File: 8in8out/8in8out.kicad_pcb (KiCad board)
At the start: 2 copper layers, 122 parts, among them IC1 ATTINY2313-P, J1 RJ45, J2 RJ45, J3 CONN_6, K110 G5T-1-12VDC, K120 G5T-1-12VDC, K130 G5T-1-12VDC, K140 G5T-1-12VDC, K150 G5T-1-12VDC, K160 G5T-1-12VDC, K170 G5T-1-12VDC, K180 G5T-1-12VDC, P1 CONN_5, P100 CONN_2, P101 CONN_2, P102 CONN_2, P103 CONN_2, P105 CONN_2, P106 CONN_2, P107 CONN_3, P109 CONN_2, P110 CONN_2, P120 CONN_2, P130 CONN_2, P140 CONN_2, P150 CONN_2, P160 CONN_2, P170 CONN_2, P180 CONN_2, P2 CONN_5, Q110 NPN, Q120 NPN, Q130 NPN, Q140 NPN, Q150 NPN, Q160 NPN, Q170 NPN, Q180 NPN, U1 74HC595, U10 OPTO-TRANSISTOR, U2 74LS165, U20 OPTO-TRANSISTOR, U30 OPTO-TRANSISTOR, U40 OPTO-TRANSISTOR, U50 OPTO-TRANSISTOR, U60 OPTO-TRANSISTOR, U70 OPTO-TRANSISTOR, U80 OPTO-TRANSISTOR

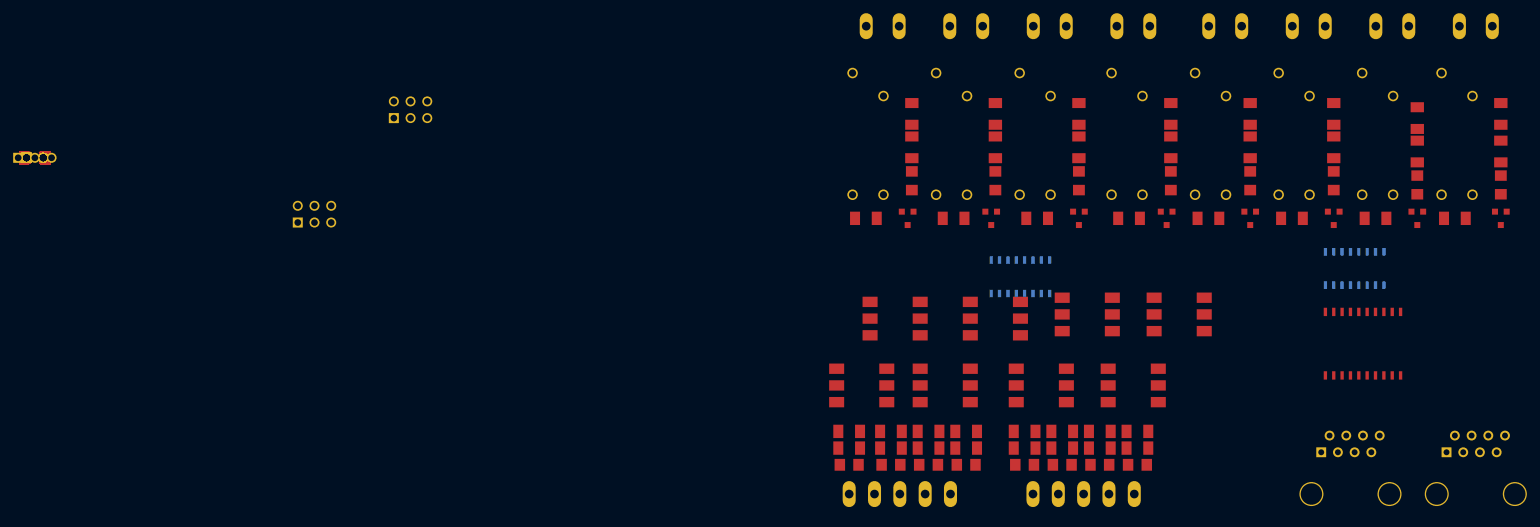
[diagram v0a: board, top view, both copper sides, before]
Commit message: Redimensionnement PCB en 100*86
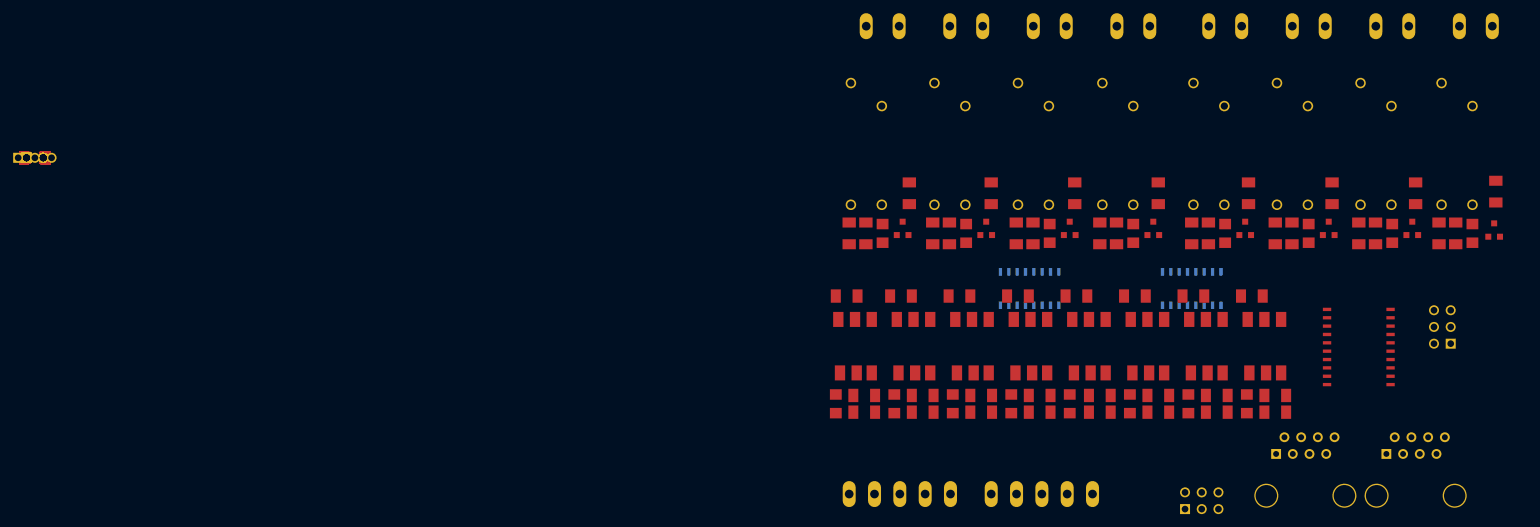
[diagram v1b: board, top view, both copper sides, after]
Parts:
- ISP0: footprint HE10-6 -> pin_array_3x2
- moved R82 186.2 mm to (247.9, 119.8)
- moved R72 177.4 mm to (239.0, 119.8)
- moved ISP0 172.3 mm to (276.9, 124.5), turned to 90 degrees
- moved R62 168.5 mm to (230.1, 119.8)
- moved R52 159.7 mm to (221.2, 119.8)
- moved R42 150.9 mm to (212.3, 119.8)
- moved R32 142.1 mm to (203.5, 119.8)
- moved J3 134.2 mm to (240.3, 150.9)
- moved R22 133.3 mm to (194.6, 119.8)
- moved R12 125.2 mm to (186.3, 119.8)
- moved U1 25.0 mm to (238.8, 118.6), turned to 180 degrees
- moved R80 21.7 mm to (251.5, 137.4), turned to 0 degrees
- moved R81 21.7 mm to (251.5, 134.9), turned to 0 degrees
- moved R141 21.1 mm to (224.8, 110.2)
- moved R111 20.5 mm to (186.7, 110.2)
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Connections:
- P1 pad 5: DGND -> GND
- P2 pad 5: DGND -> GND
- U2 pad 11: (no net) -> CMD0
- U2 pad 12: (no net) -> CMD1
- U2 pad 13: (no net) -> CMD2
- U2 pad 14: (no net) -> CMD3
- U2 pad 3: (no net) -> CMD4
- U2 pad 4: (no net) -> CMD5
- U2 pad 5: (no net) -> CMD6
- U2 pad 6: (no net) -> CMD7

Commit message: Correction pin data du 74HC165 Ajustement position des composants
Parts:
- P105: footprint PIN_ARRAY_2X1 -> MOL_CONN_2_VH
- P107: footprint PIN_ARRAY_3X1 -> PIN_ARRAY_5x1
- moved R4 235.2 mm to (297.4, 116.8)
- moved P103 215.5 mm to (275.6, 133.6), turned to 180 degrees
- moved P102 215.1 mm to (275.6, 131.1), turned to 180 degrees
- moved P101 214.8 mm to (275.6, 128.5), turned to 180 degrees
- moved R2 214.6 mm to (276.1, 123.4), turned to 180 degrees
- moved P100 214.4 mm to (275.6, 126.0), turned to 180 degrees
- moved D2 214.3 mm to (276.1, 120.9)
- moved P106 214.1 mm to (276.1, 118.4)
- moved C2 202.2 mm to (261.6, 136.1), turned to 270 degrees
- moved R1 201.7 mm to (263.9, 115.3), turned to 180 degrees
- moved C1 199.7 mm to (259.1, 136.1), turned to 270 degrees
- moved R3 197.2 mm to (256.5, 136.1), turned to 270 degrees
- moved D3 195.9 mm to (256.5, 128.3), turned to 270 degrees
- moved D1 195.9 mm to (258.1, 115.3), turned to 180 degrees
- moved P109 195.0 mm to (256.5, 121.9), turned to 270 degrees
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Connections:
- U2 pad 10: DATA_IN -> (no net)
- U2 pad 9: (no net) -> DATA_IN

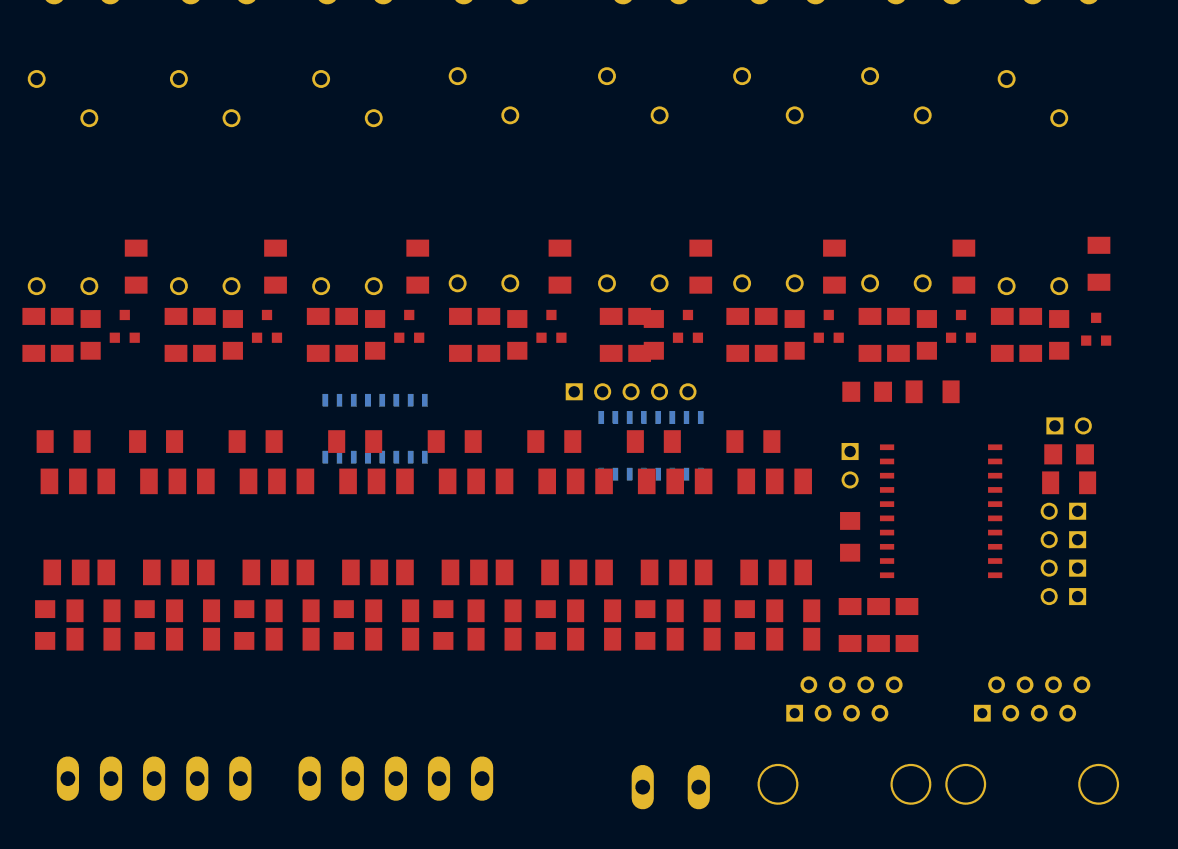
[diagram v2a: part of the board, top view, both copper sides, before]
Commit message: Modification 74HC165
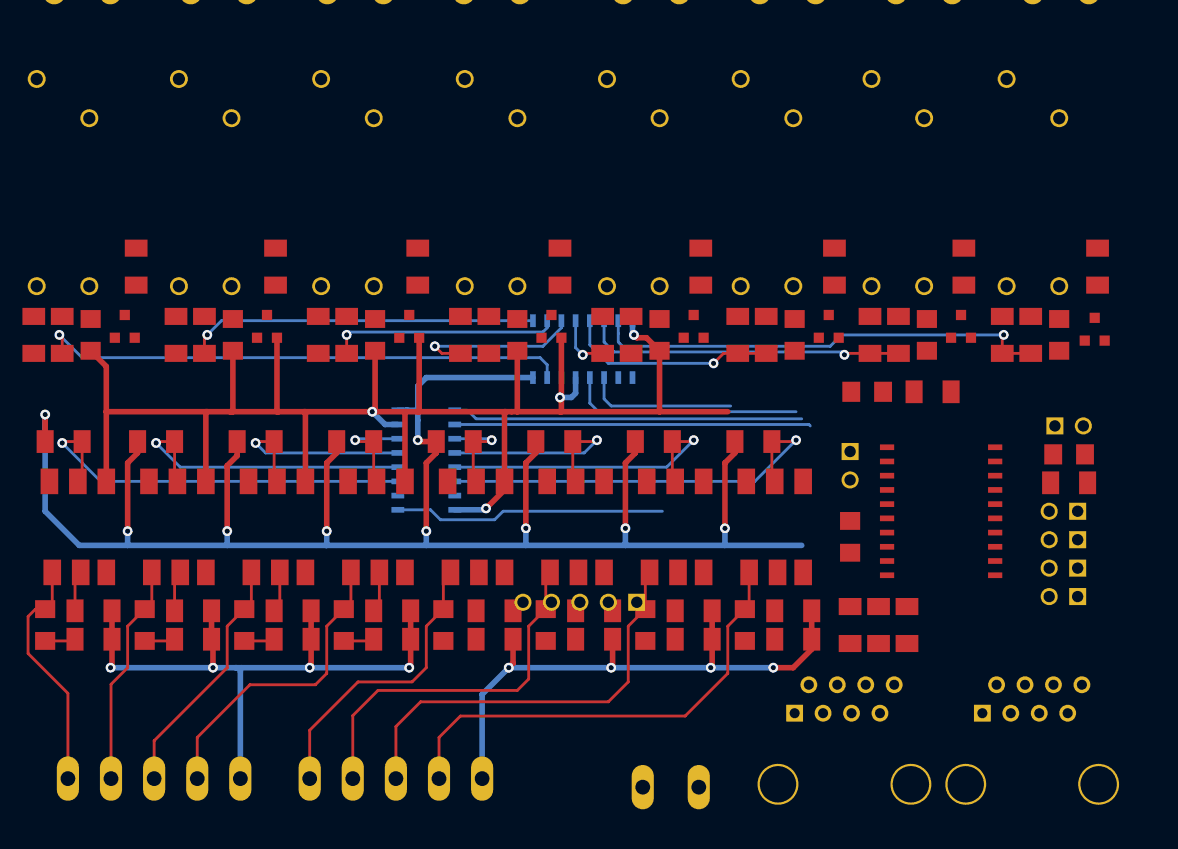
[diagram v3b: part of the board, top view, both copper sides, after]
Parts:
- moved P107 19.3 mm to (232.4, 134.1), turned to 180 degrees
- moved U1 10.6 mm to (232.7, 111.5), turned to 0 degrees
- moved U2 5.36 mm to (218.7, 121.4), turned to 270 degrees
- moved R150 0.76 mm to (237.0, 110.2)
- moved R151 0.76 mm to (234.4, 110.2)
- moved K140 0.68 mm to (221.0, 106.9)
- moved D150 0.51 mm to (239.5, 110.2)
- moved Q150 0.51 mm to (242.6, 109.5)
- moved D181 0.28 mm to (278.6, 104.1)
- moved K160 0.28 mm to (245.6, 106.9)
- moved K170 0.28 mm to (257.3, 106.9)
- moved K150 0.25 mm to (233.7, 106.9)
- moved Q180 0.13 mm to (278.4, 109.7)
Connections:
- P1 pad 5: GND -> DGND
- P2 pad 5: GND -> DGND
- R10 pad 2: GND -> DGND
- R11 pad 2: GND -> DGND
- R20 pad 2: GND -> DGND
- R21 pad 2: GND -> DGND
- R30 pad 2: GND -> DGND
- R31 pad 2: GND -> DGND
- R40 pad 2: GND -> DGND
- R41 pad 2: GND -> DGND
- R50 pad 2: GND -> DGND
- R51 pad 2: GND -> DGND
- R60 pad 2: GND -> DGND
- R61 pad 2: GND -> DGND
- R70 pad 2: GND -> DGND
- R71 pad 2: GND -> DGND
- R80 pad 2: GND -> DGND
- R81 pad 2: GND -> DGND
- U1 pad 8: GND -> DGND
- U2 pad 15: CLK_IN -> DGND
- U2 pad 8: GND -> DGND
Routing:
- net DGND: track 0.00 -> 261.5 mm, vias 0 -> 12
- net +5V: track 0.00 -> 166.9 mm, vias 0 -> 9
- net OUT0: track 0.00 -> 47.6 mm, vias 0 -> 1
- net IN7: track 0.00 -> 41.6 mm
- net OUT7: track 0.00 -> 41.1 mm, vias 0 -> 1
- net CMD7: track 0.00 -> 37.9 mm, vias 0 -> 1
- net CMD0: track 0.00 -> 36.9 mm, vias 0 -> 1
- net IN5: track 0.00 -> 33.0 mm
- net CLK_IN: track 0.00 -> 31.8 mm
- net OUT1: track 0.00 -> 31.4 mm, vias 0 -> 1
- net LATCH_IN: track 0.00 -> 31.3 mm
- net N-0000073: track 0.00 -> 29.3 mm
- net OUT6: track 0.00 -> 28.7 mm, vias 0 -> 1
- net CMD6: track 0.00 -> 28.0 mm, vias 0 -> 1
- net CMD1: track 0.00 -> 27.8 mm, vias 0 -> 1
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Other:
- net class GND added: clearance 0.254, trace_width 0.50038, via_dia 0.889, via_drill 0.635

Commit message: Routage, diverses ameliorations
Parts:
- removed D10, D110, D120, D130, D140, D150, D160, D170, D180, D20, D30, D40, D50, D60, D70, D80: LED, LED-1206
- removed P107: CONN_3, PIN_ARRAY_5x1
- removed P109: CONN_2, PIN_ARRAY_2X1
- removed R10, R110, R12, R120, R130, R140, R150, R160, R170, R180, R20, R22, R30, R32, R40, R42, R50, R52, R60, R62, R70, R72, R80, R82: R, SM1206
- removed U2: 74LS165, SO16E
- added P3: CONN_10X2, pin_array_10x2, F.Cu at (212.0, 120.4)
- added P4: CONN_2, PIN_ARRAY_2X1, F.Cu at (275.6, 130.3)
- IC1: value ATTINY2313-P -> ATTINY48-A; footprint SO20L -> TQFP32
- U1: value 74HC595 -> 78L05; footprint SO16E -> TO220_VERT; moved to F.Cu
- moved J3 35.1 mm to (265.2, 133.1), turned to 180 degrees
- moved R4 32.2 mm to (265.7, 121.9), turned to 270 degrees
- moved U1 28.6 mm to (250.4, 133.9), turned to 90 degrees
- moved ISP0 27.5 mm to (260.6, 121.9)
- moved P103 27.3 mm to (249.1, 126.9)
- moved P100 27.3 mm to (249.1, 119.3)
- moved P101 27.3 mm to (249.1, 121.9)
- moved P102 27.3 mm to (249.1, 124.4)
- moved IC1 27.0 mm to (238.0, 121.7), turned to 180 degrees
- moved D1 19.7 mm to (276.6, 121.9), turned to 270 degrees
- moved P106 17.1 mm to (287.5, 105.7)
- moved C1 16.9 mm to (268.2, 121.9)
- moved C2 16.9 mm to (270.8, 121.9)
- moved D2 16.6 mm to (292.7, 119.6), turned to 90 degrees
- moved U80 15.6 mm to (238.8, 138.4), turned to 180 degrees
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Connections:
- C1 pad 2: DGND -> GND
- C2 pad 2: DGND -> GND
- D1 pad 2: DGND -> GND
- D2 pad 2: DGND -> GND
- D3 pad 1: N-0000034 -> LED
- IC1 pad 1: N-0000043 -> A0
- IC1 pad 10: DGND -> OUT4
- IC1 pad 11: /INT -> OUT3
- IC1 pad 12: DATA_IN -> OUT2
- IC1 pad 13: A0 -> OUT1
- IC1 pad 14: A1 -> OUT0
- IC1 pad 15: A2 -> MOSI
- IC1 pad 16: A3 -> MISO
- IC1 pad 17: MOSI(SDA) -> SCK
- IC1 pad 18: MISO -> +5V
- IC1 pad 19: SCK(SCL) -> CMD7
- IC1 pad 2: RX -> A1
- IC1 pad 20: +5V -> CMD6
- IC1 pad 3: TX -> A2
- IC1 pad 4: LATCH_IN -> +5V
- IC1 pad 5: N-0000034 -> GND
- IC1 pad 6: CLK_IN -> A3
- IC1 pad 7: (no net) -> OUT7
- IC1 pad 8: (no net) -> OUT6
- IC1 pad 9: (no net) -> OUT5
- ISP0 pad 1: (no net) -> RESET
- ISP0 pad 2: DGND -> GND
- ISP0 pad 3: SCK(SCL) -> SCK
- ISP0 pad 4: MOSI(SDA) -> MOSI
- J1 pad 1: MOSI(SDA) -> SDA
- J1 pad 2: DGND -> GND
- J1 pad 3: SCK(SCL) -> SCL
- J1 pad 4: DGND -> GND
- J1 pad 6: DGND -> GND
- J1 pad 7: +5V -> 5V_EXT
- J1 pad 8: +5V -> 5V_EXT
- J2 pad 1: MOSI(SDA) -> SDA
- J2 pad 2: DGND -> GND
- J2 pad 3: SCK(SCL) -> SCL
- J2 pad 4: DGND -> GND
- J2 pad 6: DGND -> GND
- J2 pad 7: +5V -> 5V_EXT
- J2 pad 8: +5V -> 5V_EXT
- J3 pad 1: +5V -> 5V_EXT
- J3 pad 2: DGND -> GND
- J3 pad 3: SCK(SCL) -> SCL
- J3 pad 4: MOSI(SDA) -> SDA
- P1 pad 5: DGND -> COM0
- P100 pad 1: DGND -> GND
- P101 pad 1: DGND -> GND
- P102 pad 1: DGND -> GND
- P103 pad 1: DGND -> GND
- P105 pad 2: DGND -> GND
- P106 pad 2: DGND -> GND
- P2 pad 5: DGND -> COM1
- Q110 pad 1: DGND -> GND
- Q120 pad 1: DGND -> GND
- Q130 pad 1: DGND -> GND
- Q140 pad 1: DGND -> GND
- Q150 pad 1: DGND -> GND
- Q160 pad 1: DGND -> GND
- Q170 pad 1: DGND -> GND
- Q180 pad 1: DGND -> GND
- R11 pad 2: DGND -> COM0
- R21 pad 2: DGND -> COM0
- R3 pad 2: DGND -> GND
- R31 pad 2: DGND -> COM0
- R4 pad 2: N-0000043 -> RESET
- R41 pad 2: DGND -> COM0
- R51 pad 2: DGND -> COM1
- R61 pad 2: DGND -> COM1
- R71 pad 2: DGND -> COM1
- R81 pad 2: DGND -> COM1
- U1 pad 1: OUT1 -> 5V_EXT
- U1 pad 2: OUT2 -> +12V
- U1 pad 3: OUT3 -> GND
- U10 pad 4: DGND -> GND
- U20 pad 4: DGND -> GND
- U30 pad 4: DGND -> GND
- U40 pad 4: DGND -> GND
- U50 pad 4: DGND -> GND
- U60 pad 4: DGND -> GND
- U70 pad 4: DGND -> GND
- U80 pad 4: DGND -> GND
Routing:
- net DGND: track 261.5 -> 0.00 mm, vias 12 -> 0
- net +5V: track 166.9 -> 38.6 mm, vias 9 -> 0
- net 5V_EXT: track 0.00 -> 62.6 mm
- net SCL: track 0.00 -> 57.5 mm, vias 0 -> 2
- net OUT2: track 20.5 -> 76.8 mm
- net +12V: track 0.00 -> 54.8 mm
- net /INT: track 0.00 -> 54.6 mm
- net COM1: track 0.00 -> 53.4 mm
- net RESET: track 0.00 -> 53.0 mm, vias 0 -> 1
- net SDA: track 0.00 -> 51.9 mm, vias 0 -> 2
- net OUT3: track 15.2 -> 63.7 mm
- net LED: track 0.00 -> 47.4 mm, vias 0 -> 1
- net COM0: track 0.00 -> 46.7 mm
- net CMD4: track 8.72 -> 52.2 mm
- net CMD3: track 9.23 -> 52.4 mm
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
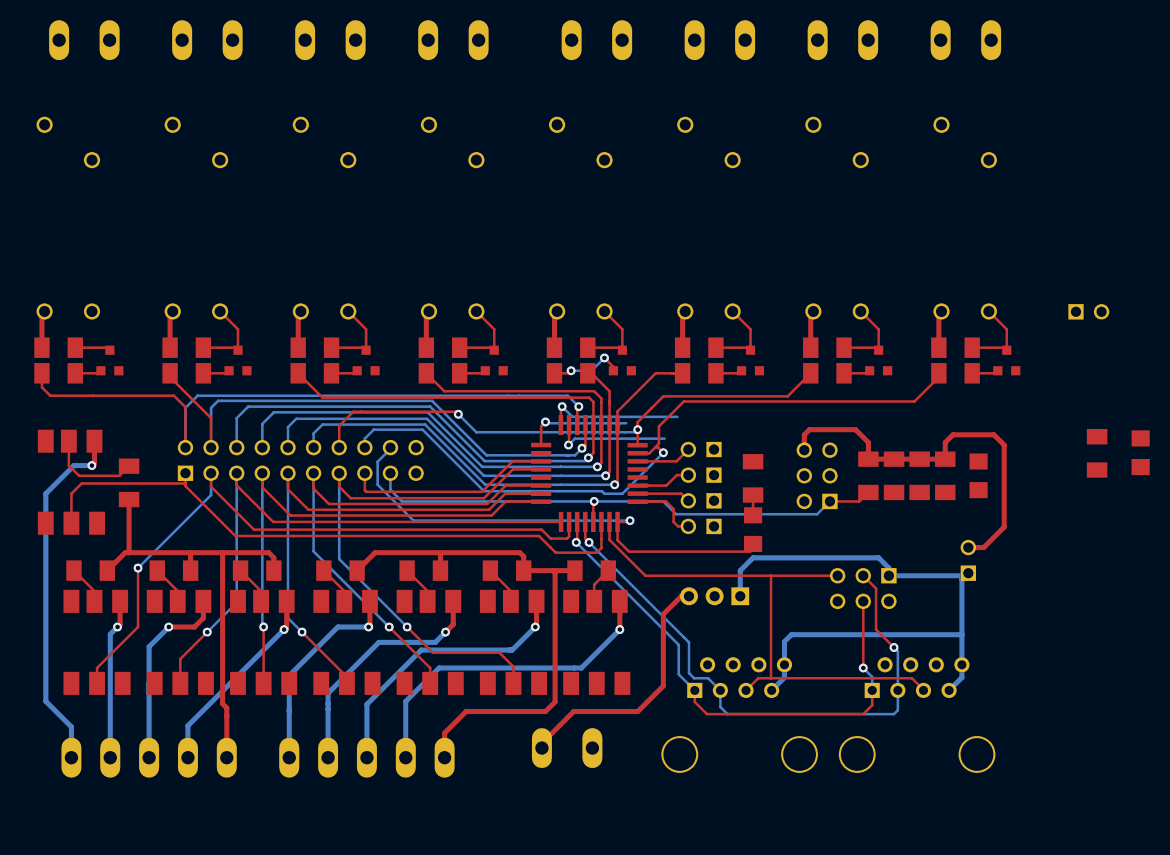
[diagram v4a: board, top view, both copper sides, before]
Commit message: Remplacement des transistors et diodes de roues libres par un ULN2803
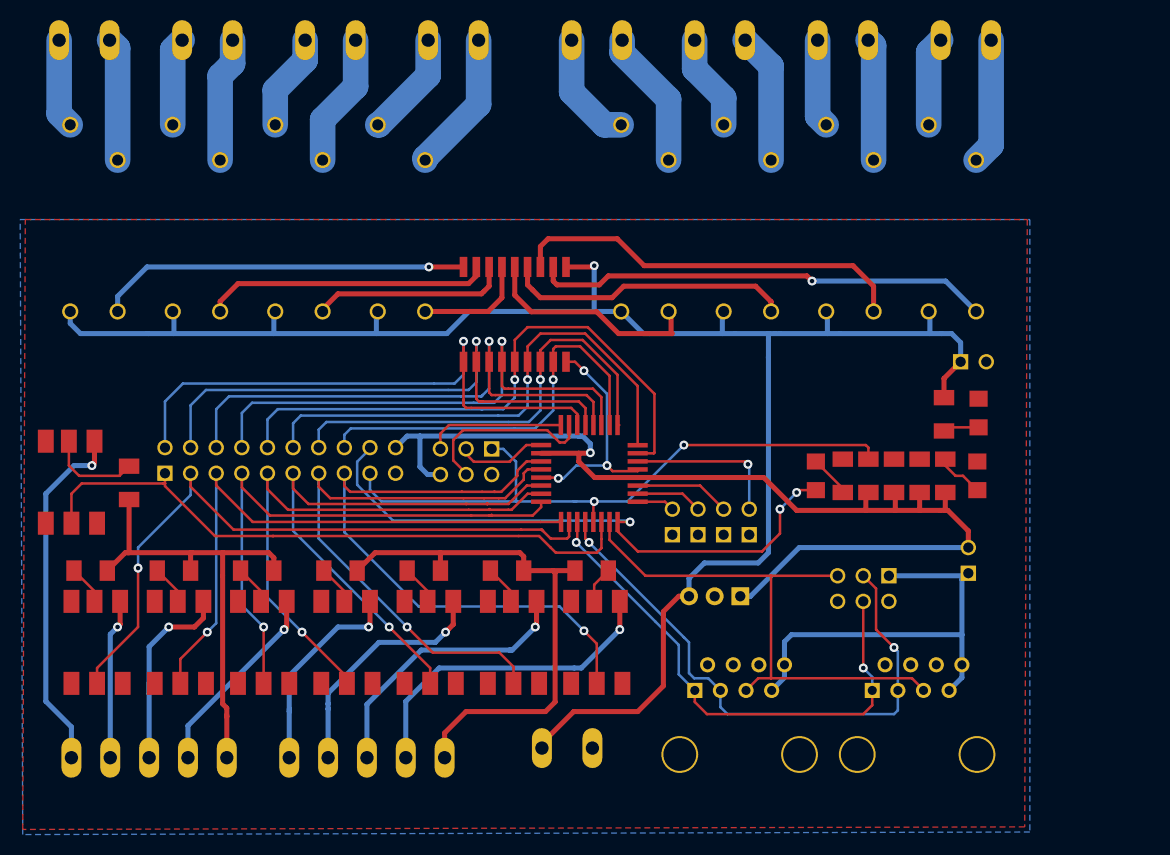
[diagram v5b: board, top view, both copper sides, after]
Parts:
- removed D111, D121, D131, D141, D151, D161, D171, D181: DIODE, SM1206
- removed Q110, Q120, Q130, Q140, Q150, Q160, Q170, Q180: NPN, SOT23EBC
- removed R111, R121, R131, R141, R151, R161, R171, R181: R, SM1206
- added U2: ULN2803, SOIC18, F.Cu at (230.6, 105.9)
- U1: value 78L05 -> 7805; footprint TO220_VERT -> TO220_7805_VERT
- moved ISP0 34.8 mm to (225.8, 120.5), turned to 180 degrees
- moved D2 16.5 mm to (276.6, 115.7)
- moved R2 15.7 mm to (273.2, 115.8)
- moved P106 12.5 mm to (276.1, 110.6)
- moved R3 8.89 mm to (263.1, 121.9)
- moved P100 8.61 mm to (253.9, 126.5), turned to 90 degrees
- moved D3 8.20 mm to (260.5, 121.9)
- moved K150 6.35 mm to (240.0, 106.7)
- moved P101 5.14 mm to (251.3, 126.5), turned to 90 degrees
- moved K140 5.08 mm to (215.9, 106.7)
- moved K160 3.81 mm to (250.2, 106.7)
- moved P103 2.89 mm to (246.3, 126.5), turned to 90 degrees
- moved K110 2.54 mm to (185.4, 106.7)
- moved K130 2.54 mm to (205.7, 106.7)
- moved P102 2.12 mm to (248.8, 126.5), turned to 90 degrees
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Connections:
- IC1 pad 10: OUT4 -> OUT7
- IC1 pad 7: OUT7 -> OUT4
- IC1 pad 8: OUT6 -> OUT5
- IC1 pad 9: OUT5 -> OUT6
- K110 pad 2: N-0000085 -> R0
- K120 pad 2: N-0000012 -> R1
- K130 pad 2: N-0000016 -> R2
- K140 pad 2: N-0000028 -> R3
- K150 pad 2: N-0000030 -> R4
- K160 pad 2: N-0000024 -> R5
- K170 pad 2: N-0000026 -> R6
- K180 pad 2: N-000008 -> R7
- P3 pad 19: +5V -> GND
- P3 pad 20: GND -> +5V
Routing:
- net +12V: track 54.8 -> 177.5 mm, vias 0 -> 1
- net +5V: track 38.6 -> 107.7 mm, vias 0 -> 1
- net R7: track 0.00 -> 45.5 mm, vias 0 -> 1
- net CMD7: track 20.5 -> 62.0 mm, vias 0 -> 1
- net R6: track 0.00 -> 39.8 mm
- net R0: track 0.00 -> 37.2 mm, vias 0 -> 1
- net OUT7: track 70.5 -> 40.8 mm
- net R5: track 0.00 -> 28.5 mm
- net R1: track 0.00 -> 28.3 mm
- net GND: track 0.00 -> 23.0 mm, vias 0 -> 3
- net R4: track 0.00 -> 22.3 mm
- net OUT2: track 76.8 -> 54.7 mm
- net R2: track 0.00 -> 19.6 mm
- net 5V_EXT: track 62.6 -> 43.6 mm
- net /230_140_1: track 0.00 -> 14.1 mm
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- added copper zone on B.Cu, net GND
- added copper zone on F.Cu, net GND
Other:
- net class +230 1mm: clearance 0.254 -> 1.50114
- net class +230V: clearance 0.254 -> 0.508; trace_width 0.7493 -> 2.54
